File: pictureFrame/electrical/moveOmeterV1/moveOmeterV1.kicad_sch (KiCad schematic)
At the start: 0 parts

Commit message: Add device settings, fix time format persistence, update landing page content
Mobile App Improvements:
- Add device settings page with room name editing and sensor tuning parameters
  - Human detection thresholds (seated/motion distance)
  - Fall detection timing (sensitivity, fall time, residence time)
  - Sampling intervals for all modes
- Fix 12-hour/24-hour time format persistence across all pages
- Make "Today's Activity" section clickable to view full 24-hour detail
- Fix room name persistence when edited in settings
- Change device list to show "Last motion:" with actual time from daily metrics
- Add day detail page for viewing historical 24-hour data

Landing Page Updates:
- Update "Who" tab: add "a real human", update job history wording
- Update "What" tab: add cellular modem info, plug-and-play setup details
- Update "Why" tab: refine wording, link to Who tab instead of contact
- Update "How" tab: simplify pricing to generic monthly fee and rental option
- Add contact page with HubSpot form integration
- Deploy landing page and contact page to production

Database Automation:
- Add daily metrics calculation automation with pg_cron
- Create two scheduled jobs: yesterday's final metrics (6 AM) and today's live updates (every 15 min)
- Add comprehensive automation documentation

Hardware & Firmware:
- Update KiCad PCB design files
- Add mmWave sensor footprints and symbols
- Update firmware BLE provisioning

Co-Authored-By: Claude Sonnet 4.5 <noreply@anthropic.com>
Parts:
- added A1: Adafruit_Feather_HUZZAH32_ESP32, Module:Adafruit_Feather, symbol MCU_Module:Adafruit_Feather_HUZZAH32_ESP32
- added C1: 100uF, symbol Device:C_Polarized
- added C2: 0.1uF, symbol Device:C_Small
- added C3: C_Small, symbol Device:C_Small
- added U1: SEN0623, Module:MODULE_SEN0623, symbol Interface:SEN0623
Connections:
- new net: A1.26 (USB), C1.1, C2.1, C3.1, U1.1 (VIN)
- new net: A1.14 (RX/IO16), U1.3 (RX)
- new net: A1.15 (TX/IO17), U1.4 (TX)
- new net: A1.5 (DAC2/A0), U1.5 (IO1)
- new net: A1.6 (DAC1/A1), U1.6 (IO2)
- new net GND: A1.4 (GND), C1.2, C2.2, C3.2, U1.2 (GND)

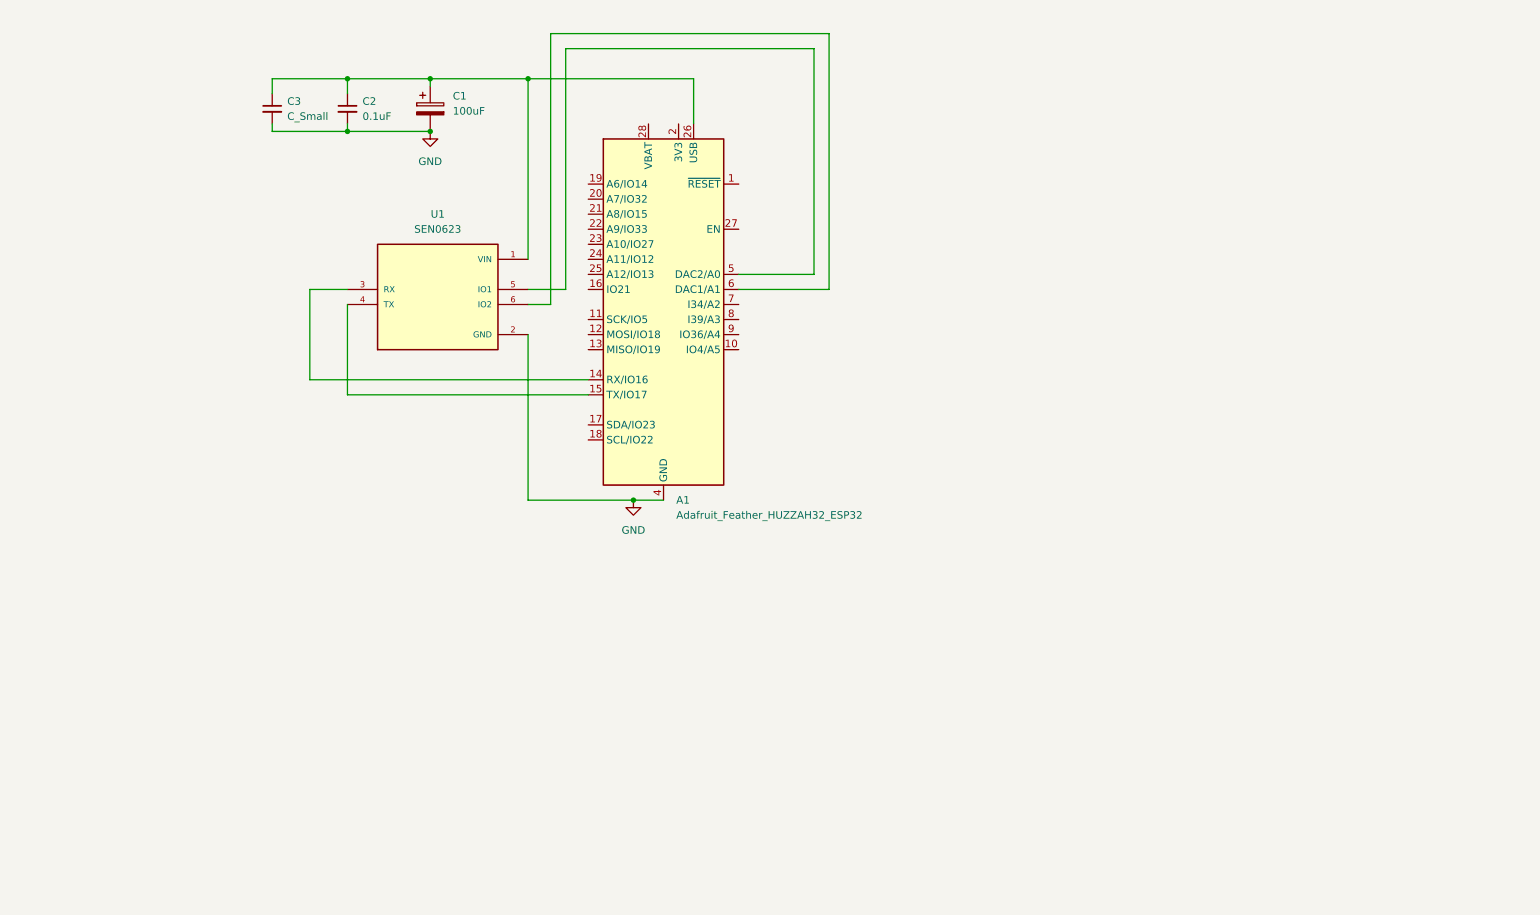
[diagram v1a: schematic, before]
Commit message: Hardware: KiCad PCB v1 updates, hardware v0.01 files, new part libraries
- Update moveOmeterV1 schematic and PCB layout
- Add STEP export files (moveOmeterV1.step, moveOmeterV1_fused.step)
- Remove stale lock files and auto-saved backup files
- Add hardware version 0.01 files (2026-04-06)
- Add Adafruit ESP32-C6 and Eagle KiCad part libraries

Co-Authored-By: Claude Sonnet 4.6 <noreply@anthropic.com>
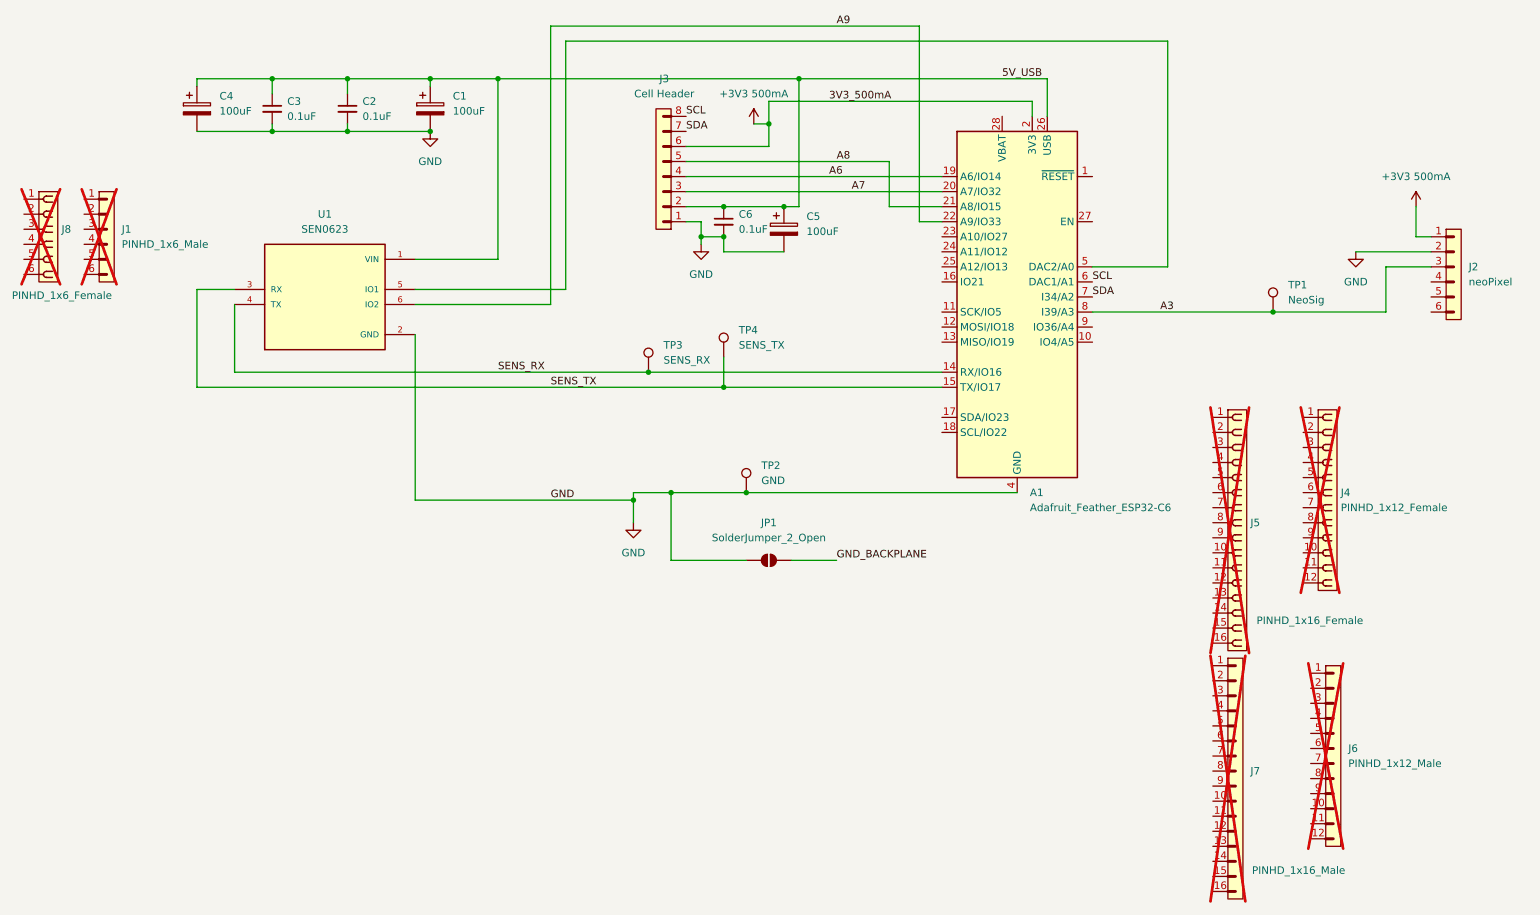
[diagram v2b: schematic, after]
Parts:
- added C4, C5: 100uF, Capacitor_THT:CP_Radial_D8.0mm_P3.50mm, symbol Device:C_Polarized
- added C6: 0.1uF, Capacitor_THT:C_Disc_D3.0mm_W2.0mm_P2.50mm, symbol Device:C_Small
- added J1: PINHD_1x6_Male, Connector_PinHeader_2.54mm:PinHeader_1x06_P2.54mm_Vertical, symbol PCM_SL_Pin_Headers:PINHD_1x6_Male
- added J2: neoPixel, Module:neoPixel6pin, symbol PCM_SL_Pin_Headers:PINHD_1x6_Male
- added J3: Cell Header, Connector_PinHeader_2.54mm:PinHeader_1x08_P2.54mm_Vertical, symbol PCM_SL_Pin_Headers:PINHD_1x8_Male
- added J4: PINHD_1x12_Female, Connector_PinSocket_2.54mm:PinSocket_1x12_P2.54mm_Vertical, symbol PCM_SL_Pin_Headers:PINHD_1x12_Female
- added J5: PINHD_1x16_Female, Connector_PinSocket_2.54mm:PinSocket_1x16_P2.54mm_Vertical, symbol PCM_SL_Pin_Headers:PINHD_1x16_Female
- added J6: PINHD_1x12_Male, Connector_PinHeader_2.54mm:PinHeader_1x12_P2.54mm_Vertical, symbol PCM_SL_Pin_Headers:PINHD_1x12_Male
- added J7: PINHD_1x16_Male, Connector_PinHeader_2.54mm:PinHeader_1x16_P2.54mm_Vertical, symbol PCM_SL_Pin_Headers:PINHD_1x16_Male
- added J8: PINHD_1x6_Female, Connector_PinSocket_2.54mm:PinSocket_1x06_P2.54mm_Vertical, symbol PCM_SL_Pin_Headers:PINHD_1x6_Female
- added JP1: SolderJumper_2_Open, Jumper:SolderJumper-2_P1.3mm_Open_RoundedPad1.0x1.5mm, symbol Jumper:SolderJumper_2_Open
- added TP1: NeoSig, TestPoint:TestPoint_Loop_D2.60mm_Drill1.6mm_Beaded, symbol Connector:TestPoint
- added TP2: GND, TestPoint:TestPoint_Loop_D2.60mm_Drill1.6mm_Beaded, symbol Connector:TestPoint
- added TP3: SENS_RX, TestPoint:TestPoint_Loop_D2.60mm_Drill1.6mm_Beaded, symbol Connector:TestPoint
- added TP4: SENS_TX, TestPoint:TestPoint_Loop_D2.60mm_Drill1.6mm_Beaded, symbol Connector:TestPoint
- A1: value Adafruit_Feather_HUZZAH32_ESP32 -> Adafruit_Feather_ESP32-C6; Manufacturer (none) -> Adafruit Industries LLC; Manufacturer Link (none) -> https://learn.adafruit.com/adafruit-esp32-c6-feather/pinouts; Manufacturer Part # (none) -> 5933; Price (none) -> 14.95; Vendor Link (none) -> https://www.digikey.com/short/d5h8qbz2; Vendor Part # (none) -> 1528-5933-ND
- C1: footprint (none) -> Capacitor_THT:CP_Radial_D8.0mm_P3.50mm; Manufacturer (none) -> Panasonic Electronic Components; Manufacturer Part # (none) -> ECE-A1EN101U; Price (none) -> 0.84; Vendor Link (none) -> https://www.digikey.com/short/4pp2b8f4; Vendor Part # (none) -> P1180-ND
- C2: footprint (none) -> Capacitor_THT:C_Disc_D3.0mm_W2.0mm_P2.50mm; Manufacturer (none) -> KYOCERA AVX; Manufacturer Part # (none) -> SR205C104KAR; Price (none) -> 0.42; Vendor Link (none) -> https://www.digikey.com/short/vqwr03z3; Vendor Part # (none) -> 478-3187-ND
- C3: value C_Small -> 0.1uF; footprint (none) -> Capacitor_THT:C_Disc_D3.0mm_W2.0mm_P2.50mm; Manufacturer (none) -> KYOCERA AVX; Manufacturer Part # (none) -> SR205C104KAR; Price (none) -> 0.42; Vendor Link (none) -> https://www.digikey.com/short/vqwr03z3; Vendor Part # (none) -> 478-3187-ND
- U1: CREATOR ANA -> (none); MANUFACTURER DFRobot -> (none); Manufacturer (none) -> DFRobot; Manufacturer Part # (none) -> SEN0623; PARTREV NA -> (none); Price (none) -> 35.00; STANDARD Manufacturer Recommendations -> (none); Vendor Link (none) -> https://www.digikey.com/short/z94w32br; Vendor Part # (none) -> 1738-SEN0623-ND
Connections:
- net GND: now also C4.2, C5.2, C6.2, J2.2, J3.1, JP1.1 (A), TP2.1
- net 5V_USB: now reaches A1.26 (USB), C1.1, C2.1, C3.1, U1.1 (VIN)
- net 5V_USB: now also C4.1, C5.1, C6.1, J3.2
- net SENS_RX: now reaches A1.14 (RX/IO16)
- net SENS_RX: now also U1.4 (TX), TP3.1; no longer U1.3 (RX)
- net SENS_TX: now reaches A1.15 (TX/IO17)
- net SENS_TX: now also U1.3 (RX), TP4.1; no longer U1.4 (TX)
- net A6: now reaches A1.19 (A6/IO14)
- net A6: now also J3.4
- net +3V3 500mA: now reaches A1.2 (3V3)
- net +3V3 500mA: now also J2.1, J3.6
- net A7: now reaches A1.20 (A7/IO32)
- net A7: now also J3.3
- net A8: now reaches A1.21 (A8/IO15)
- net A8: now also J3.5
- net A9: now reaches A1.22 (A9/IO33)
- net A9: now also U1.6 (IO2)
- net SCL: now reaches A1.6 (DAC1/A1)
- net SCL: now also J3.8; no longer U1.6 (IO2)
- net SDA: now reaches A1.7 (I34/A2)
- net SDA: now also J3.7
- net A3: now reaches A1.8 (I39/A3)
- net A3: now also J2.3, TP1.1
- new net GND_BACKPLANE: JP1.2 (B)
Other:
- moved on the sheet: A1, U1
